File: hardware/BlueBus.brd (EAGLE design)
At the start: 90 x 60 mm, 132 parts, among them Q1 NMOSFET-BSS138K, Q2 PMOSFET-DMP32D4S, Q3 NMOSFET-BSS138K, X1 CRYSTAL-12MHZ

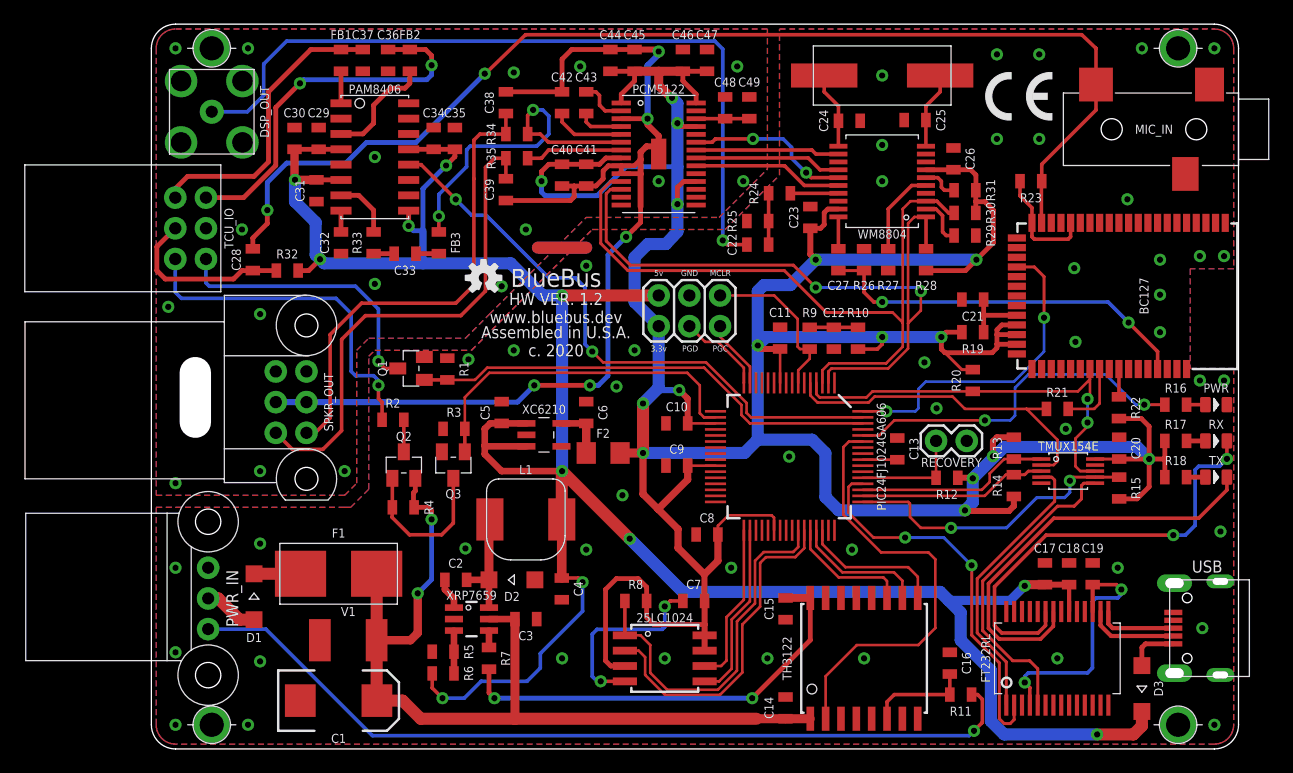
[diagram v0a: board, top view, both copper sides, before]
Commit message: [IMP] hardware: v1.5 High Voltage improvements * Remove XRP6759 * Remove Old Tantalum C1 * Remove V1 * Remove L1 * Add common mode choke at input (L1) to filter out A/C * Add new Aluminum Polymer input Capacitor rated for 35v (C1) * Add MPQ4420 wide input voltage switching regulator for 12v -> 5v regulation * Add XC6702 to protect Q2 from trancients and provide a constant voltage to TEL ON and Microphone power * Power Microphone through 12v rail * Rewire 3.3v net * Rewire 5v net * Fix decoupling cap positioning for PIC24
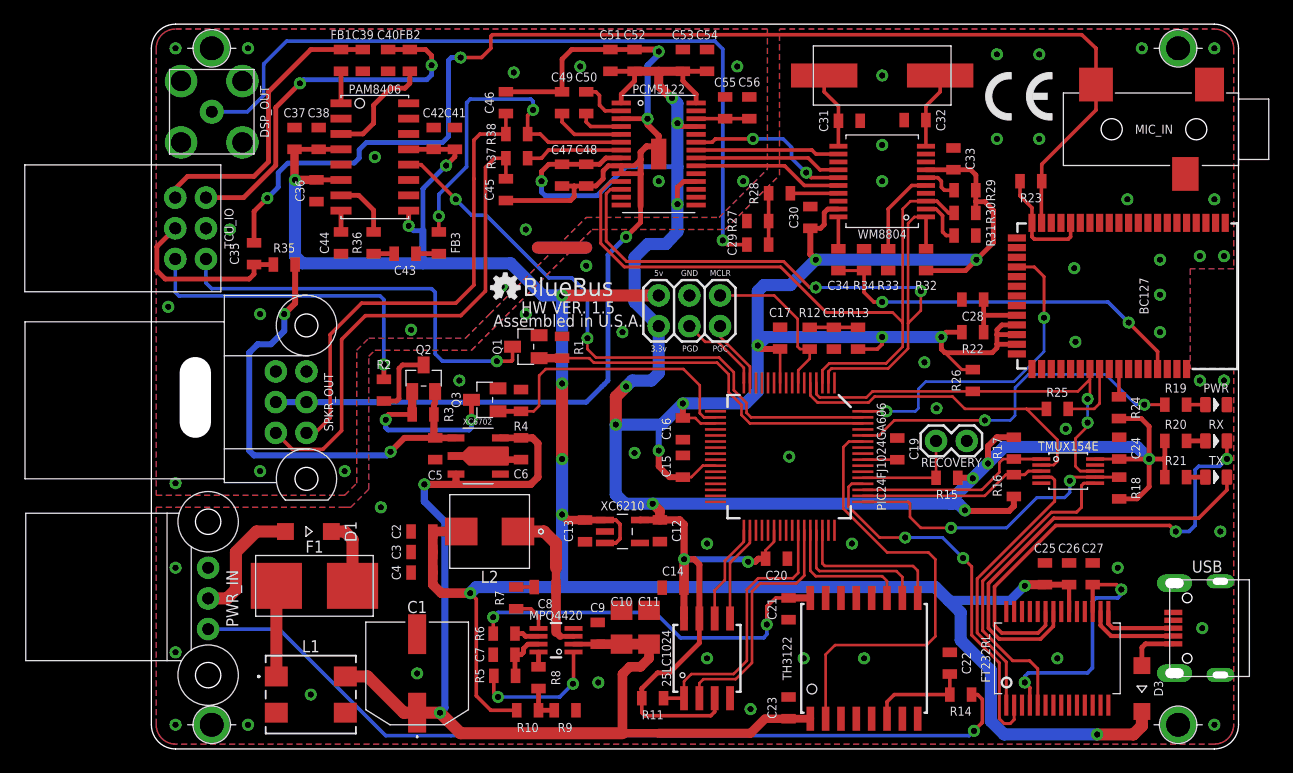
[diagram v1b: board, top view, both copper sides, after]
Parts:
- removed D2: 2A/100V, Passives:SOD123
- removed F2: 0468.500NR, Passives:1206
- removed OSHW: (no value), SparkFun-Aesthetics:OSHW-LOGO-S
- removed V1: V18AUMLA1812H, Passives:1812
- removed XRP7659: XRP7659SOT23-6, ICs:SOT23-6
- added C50: 2.2uF, Passives:0805
- added C51, C54, C56: 10uF, Passives:0805
- added C52, C53, C55: 0.1uF, Passives:0805
- added L2: ETQ-P4M100KFN, Passives:PCC-M0648M-LE
- added MPQ4420: MPQ4420, ICs:TSOT23-8
- added R36: 18k, Passives:0805
- added R37, R38: 100, Passives:0805
- added U$1: (no value), SparkFun-Aesthetics:OSHW-LOGO-MINI
- added XC6702: XC6702DC018PR-G, ICs:SOT-89-5
- C1: value 100uF -> RHS1V101MCN1GS; device Passives:EIA7343 -> Passives:RHS1V101MCN1GS
- C10, C11: value 0.1uF -> 10uF; device Passives:0805 -> Passives:1206
- C12: value 0.1uF -> 1uF
- C13, C44: value 10uF -> 1uF
- C14: value 47nF -> 0.1uF
- C15: value 2.2uF -> 0.1uF
- C16: value 0.0001UF -> 0.1uF
- C18, C29: value 10uF -> 0.1uF
- C19, C41: value 0.1uF -> 10uF
- C2: value 0.01uF -> 22uF
- C21: value 4.7uF -> 2.2uF
- C22: value 0.1uF -> 0.0001UF
- C23: value 0.1uF -> 47nF
- C24, C25: value 20pF -> 0.1uF
- C26: value 1uF -> 10uF
- C28: value 47UF -> 4.7uF
- C3: value 10uF -> 22uF
- C30, C34: value 1uF -> 0.1uF
- C31, C32: value 1uF -> 20pF
- C35: value 10uF -> 47UF
- C36: value 220pF -> 1uF
- C37: value 220pF -> 10uF
- C38: value 9nF -> 1uF
- C39: value 9nF -> 220pF
- C4: value 22uF -> 0.1uF
- C40: value 10uF -> 220pF
- C42, C43: value 2.2uF -> 1uF
- C45, C46: value 0.1uF -> 10nF
- C49: value 10uF -> 2.2uF
- C5: value 1uF -> 2.2uF
- L1: value 4.7uH -> ACM70V-701-2PL-TL00; device Passives:MPLCG0630 -> Passives:ACM70V-701-2PL-TL00
- R10: value 10k -> 41.2KOHM
- R11: value 10 -> 4.7k
- R12: value 10k -> 210
- R14: value 100k -> 10
- R15: value 100k -> 10k
- R16, R18: value 2k -> 100k
- R17: value 2k -> 10k
- R19: value 2 -> 2k
- R20, R21: value 10k -> 2k
- R22: value 10k -> 2
- R24: value 210 -> 10k
- R25: value 110 -> 10k
- R26: value 75 -> 10k
- R27: value 10k -> 110
- R28: value 4.7k -> 210
- R33: value 18k -> 10k
- R34: value 110 -> 75
- R35: value 110 -> 4.7k
- R5: value 9.09k -> 100k
- R6: value 47k -> 100k
- R7: value 100k -> 20OHM
- R8: value 4.7k -> 51KOHM
- R9: value 210 -> 7.68KOHM
- moved C28 59.7 mm to (68.0, 37.2), turned to 180 degrees
- moved R32 52.9 mm to (64.1, 40.5), turned to 90 degrees
- moved C32 48.6 mm to (63.2, 52.1), turned to 180 degrees
- moved C33 46.1 mm to (66.4, 48.9), turned to 90 degrees
- moved C31 44.5 mm to (57.8, 52.0), turned to 0 degrees
- moved R33 42.6 mm to (61.0, 40.5)
- moved C30 41.2 mm to (54.5, 44.0)
- moved R10 41.2 mm to (31.1, 3.20), turned to 180 degrees
- moved C23 40.6 mm to (52.8, 3.40)
- moved C29 39.3 mm to (50.2, 41.8), turned to 0 degrees
- moved C25 39.1 mm to (74.0, 14.5), turned to 90 degrees
- moved C22 38.1 mm to (66.1, 7.10), turned to 90 degrees
- moved R9 36.9 mm to (34.2, 3.20), turned to 180 degrees
- moved C26 35.7 mm to (76.0, 14.5)
- moved C24 35.1 mm to (80.1, 24.9), turned to 90 degrees
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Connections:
- net 12V_VIN renamed VBAT
- net VIN_DIODE renamed VBAT_DIODE
- removed net RAW_3.3V: C6.1, F2.1, XC6210.5
- new net 12V: C5.1, Q2.2, R3.2, R35.1, XC6702.1
- new net 5VREG_BS_CAP: C8.1, R7.2
- new net 5VREG_FB_T: R10.1, R8.1, R9.2
- new net 5VREG_PG: MPQ4420.1, R5.1
- new net 5VREG_VCC: C7.1, MPQ4420.7, R5.2
- new net VBAT_FUSE: F1.OUT, L1.1
- net 3.3V: now also C12.1, C14.1, C15.2, C16.2, C17.2, C20.2, C24.1, C30.1, C33.1, C48.1, C51.1, C52.1, C53.1, C54.1, R11.2, R16.2, R17.1, R21.2, R24.2, R26.2, R29.1, R32.1, XC6210.5; no longer C10.2, C11.2, C20.1, C23.1, C26.1, C40.1, C41.1, C44.1, C45.1, C46.1, C7.1, C8.2, C9.2, F2.2, R10.1, R12.2, R14.2, R17.2, R19.2, R28.1, R31.1, R8.2
- net 5V: now also C13.1, C2.1, C25.1, C26.1, C3.1, C36.1, C37.1, C38.1, C41.1, C42.1, L2.2, R10.2; no longer C17.1, C18.1, C29.1, C30.1, C31.1, C34.1, C35.1, C5.1, L1.2, R32.1, R6.2
- net 5VREG_BS: now also MPQ4420.5, R7.1; no longer C2.1, XRP7659.1
- net 5VREG_EN: now also MPQ4420.6, R6.1; no longer R7.2, XRP7659.4
- net 5VREG_FB: now also MPQ4420.8, R8.2; no longer R5.1, R6.1, XRP7659.3
- net 5VREG_SW: now also C8.2, L2.1, MPQ4420.3; no longer C2.2, D2.C, L1.1, XRP7659.6
- net AGND: now also C46.2, C47.2, C48.2, C49.1, C51.2, C52.2; no longer C38.2, C39.2, C40.2, C41.2, C42.1, C44.2
- net BT_3V3_FILTER: now also C28.1, R22.1; no longer C21.1, R19.1
- net BT_DOUT: now also C34.2, R34.2; no longer C27.2, R26.2
- net BT_MIC_L: now also C35.1; no longer C28.1
- net BT_RST: now also R24.1; no longer R22.1
- net BT_URX: now also R25.1; no longer R21.1
- net BT_URX_RES: now also R25.2; no longer R21.2
- net BT_UTX: now also R26.1; no longer R20.1
- net DAC_CAPM: now also C50.2; no longer C43.2
- net DAC_CAPP: now also C50.1; no longer C43.1
- net DAC_LDOO: now also C55.1, C56.1; no longer C48.1, C49.1
- net DAC_OUT_L: now also R38.1; no longer R34.1
- net DAC_OUT_R: now also R37.1; no longer R35.1
- net DAC_VNEG: now also C49.2; no longer C42.2
- net EE_CS: now also R11.1; no longer R8.1
- net GND: now also C1.2, C10.2, C11.2, C16.1, C17.1, C2.2, C20.1, C21.1, C22.2, C27.2, C28.2, C33.2, C38.2, C39.2, C40.2, C41.2, C42.2, C44.2, C53.2, C54.2, C55.2, C56.2, C9.2, L1.2, L1.3, MPQ4420.4, R31.1, R33.1, R34.1, R4.1, R9.1, XC6702.2; no longer C1.C, C10.1, C11.1, C16.2, C17.2, C20.2, C21.2, C29.2, C34.2, C35.2, C46.2, C47.2, C48.2, C49.2, C8.1, C9.1, D2.A, R25.1, R26.1, R29.1, R3.1, R5.2, V1.1, XRP7659.2
- net IBUS: now also R14.1; no longer R11.1
- net IBUS_5V: now also C21.2, R6.2; no longer C15.2, R7.1
- net IBUS_FILT: now also C22.1, R14.2; no longer C16.1, R11.2
- net MCU_MCLR: now also R12.2; no longer R9.2
- net MCU_MCLR_RES: now also C18.1, R12.1, R13.2; no longer C12.1, R10.2, R9.1
- net MCU_ON_LED: now also R19.2; no longer R16.2
- net MCU_ON_LED_RES: now also R19.1; no longer R16.1
- net MCU_RECOV: now also R15.1; no longer R12.1
- net MCU_SCK3: now also R32.2; no longer R28.2
- net MCU_TEL_ON: now also R4.2; no longer R3.2
- net MCU_URX: now also R16.1; no longer R14.1
- net MCU_UTX: now also R18.1; no longer R15.1
- net MCU_VCAP: now also C19.1; no longer C13.1
- net RX_LED_RES: now also R20.1; no longer R17.1
- net SPDIF_OUT: now also C29.1; no longer C22.1
- net SPDIF_RX: now also C34.1; no longer C27.1
- net SPKR_OUT_L: now also C46.1, R38.2; no longer C38.1, R34.2
- net SPKR_OUT_R: now also C45.1, R37.2; no longer C39.1, R35.2
- net SYS_3V3: now also C27.1; no longer C19.1
- net SYS_UART_SEL: now also R17.2; no longer R13.2
- net TEL_AMP_IN: now also C43.1; no longer C33.1
- net TEL_AMP_INL: now also R36.2; no longer R33.2
- net TEL_AMP_INL_CAP_RES: now also C43.2, R36.1; no longer C33.2, R33.1
- net TEL_AMP_VREF: now also C44.1; no longer C32.1
- net TEL_MIC_L_OUT: now also C35.2, R35.2; no longer C28.2, R32.2
- net TEL_ON_EN: now also R3.1; no longer R4.1
- net TEL_OUT_L+: now also C39.1; no longer C37.1
- net TEL_OUT_L-: now also C40.1; no longer C36.1
- net TX_LED_RES: now also R21.1; no longer R18.1
- net VIN: now also C1.1, C10.1, C11.1, C23.1, C6.1, C9.1, L1.4, MPQ4420.2, XC6702.3, XC6702.5; no longer C1.A, C14.1, C3.1, F1.OUT, Q2.2, R4.2, V1.2, XRP7659.5
- net WM_CSB: now also R33.2; no longer R27.2
- net WM_GPO0: now also R31.2; no longer R29.2
- net WM_RESETB: now also R29.2; no longer R31.2
- net WM_SPDIF_TX_RES: now also R28.2; no longer R24.2
- net WM_SPDIF_TX_RES2: now also C29.2, R27.2, R28.1; no longer C22.2, R24.1, R25.2
- net WM_XIN: now also C31.1; no longer C24.1
- net WM_XOP: now also C32.1; no longer C25.1
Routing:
- net 12V: track 0.00 -> 39.4 mm, vias 0 -> 2
- net VIN: track 75.7 -> 92.4 mm
- net 5VREG_PG: track 0.00 -> 11.2 mm, vias 0 -> 2
- net TEL_MUTE_IO: track 23.3 -> 34.2 mm
- net GND: track 24.2 -> 13.5 mm, vias 67 -> 65
- net MCU_TEL_MUTE: track 39.1 -> 30.4 mm
- net 3.3V: track 316.7 -> 325.1 mm, vias 16 -> 20
- net EE_CS: track 31.2 -> 23.3 mm
- net VBAT_FUSE: track 0.00 -> 7.50 mm
- net EE_SO: track 28.2 -> 20.8 mm
- net EE_SI: track 14.8 -> 7.98 mm
- net VBAT: track 4.53 -> 10.5 mm
- net EE_SCK: track 13.4 -> 8.30 mm
- net MCU_TEL_ON: track 29.0 -> 23.9 mm
- net IBUS_5V: track 36.3 -> 31.4 mm
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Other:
- board text added: "HW VER. 1.5"
- board text removed: "HW VER. 1.2"
- board text removed: "c. 2020"
- board text removed: "www.bluebus.dev"
